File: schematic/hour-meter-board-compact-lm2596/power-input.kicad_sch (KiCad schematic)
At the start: 24 parts, among them J101 VIN 9-36V, U101 LM2596S-ADJ

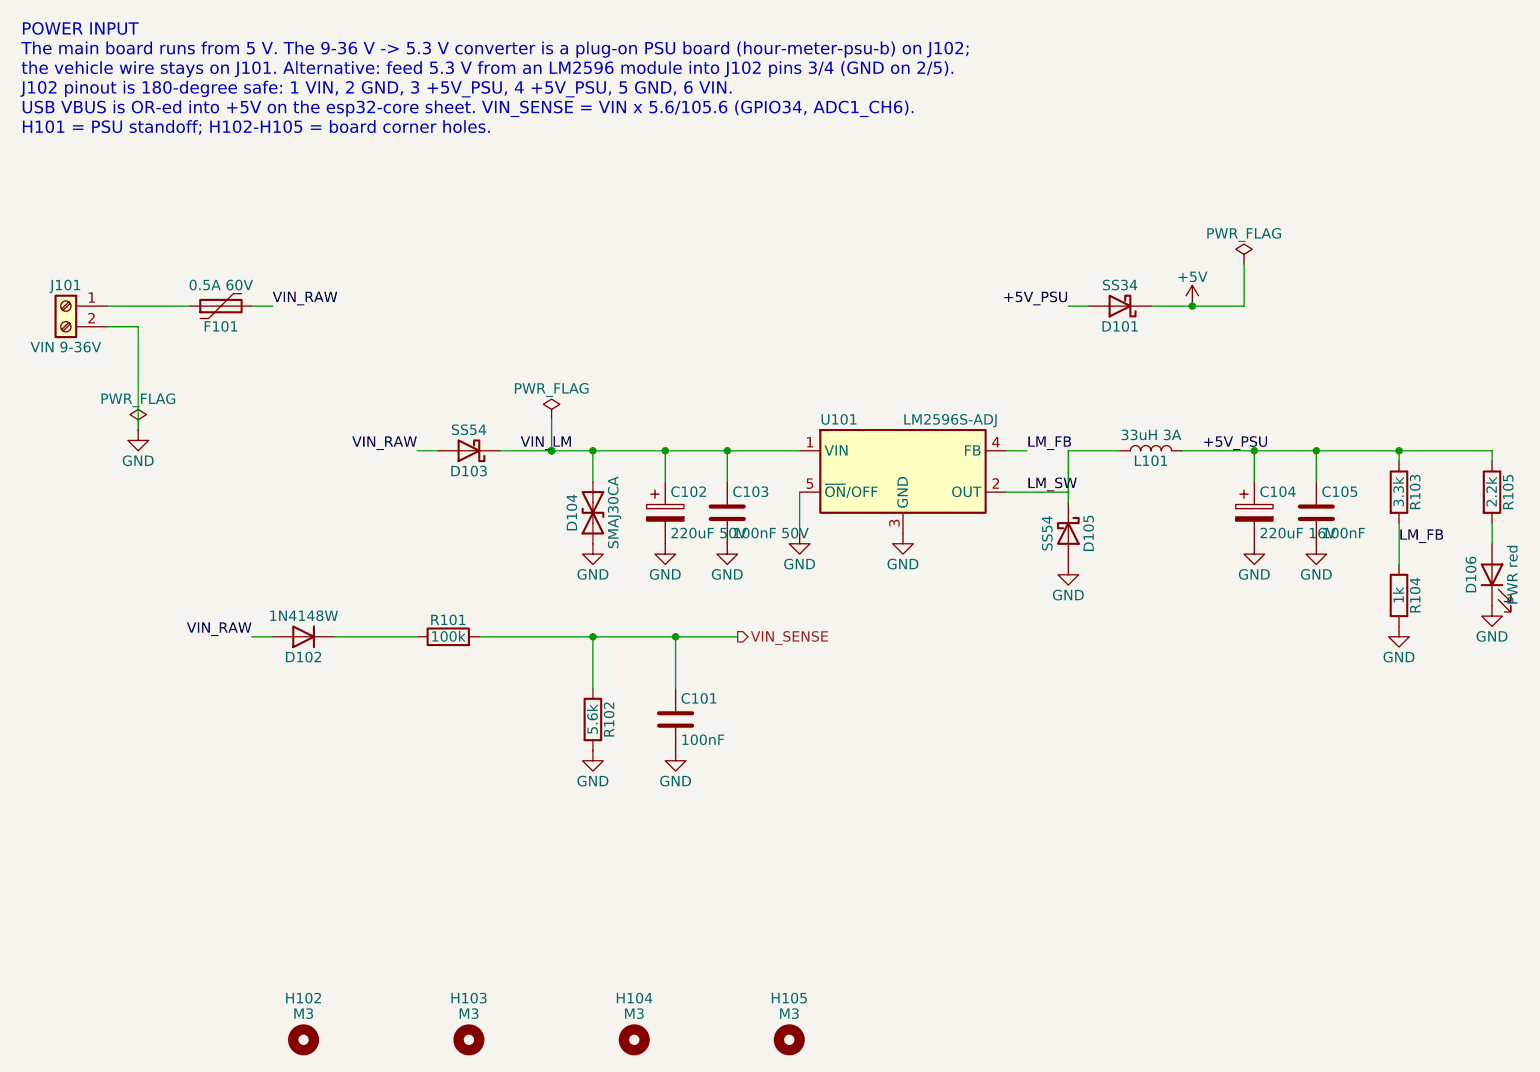
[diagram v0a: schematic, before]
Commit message: feat(pcb): use JST VH field connectors on the LM2596 compact board
- J101 (VIN 9-30V), J301 (vehicle IN), J701 (RS485) and J801 (UART) are
  latching JST VH headers instead of screw terminals and JST XH
- add TP101 VIN solder pads in parallel with J101
- GPS J802 becomes a 1x5 male pin header
- re-route the board (U203 VBUS escape fixed by re-routing the USB and
  ESP32 lines under it) and regenerate the JLCPCB order files
- tools-pcb.py: `models` command fetches the JLCPCB/EasyEDA STEP models;
  the downloaded 3d/ folders are git-ignored
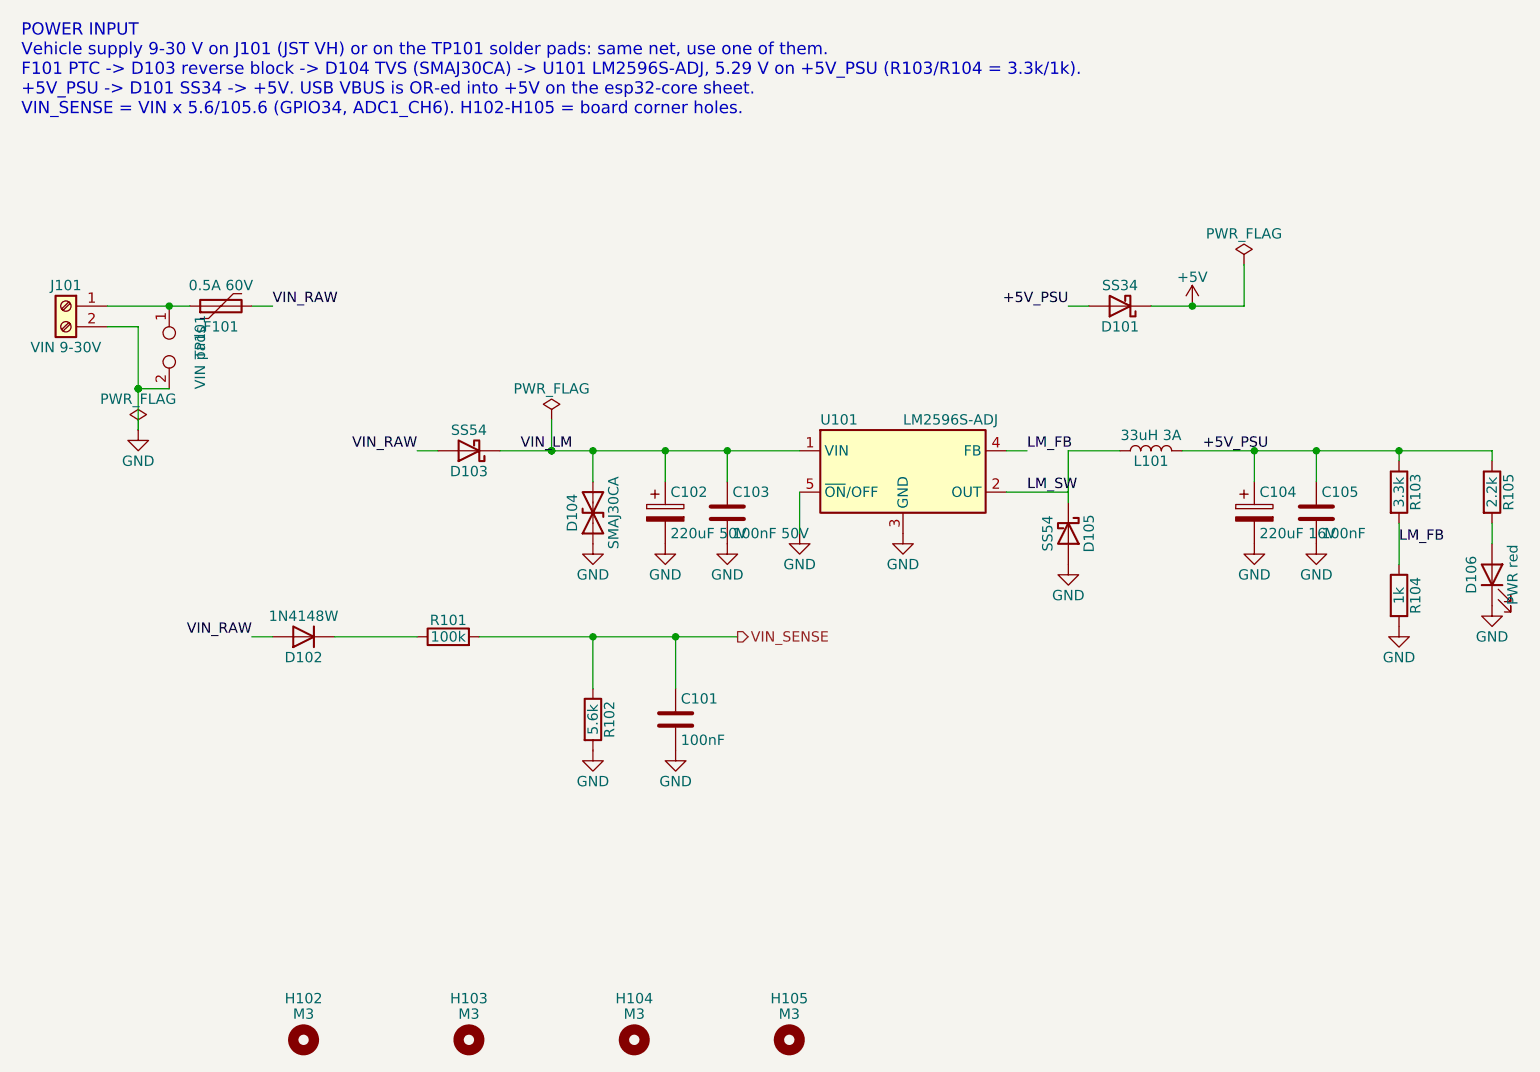
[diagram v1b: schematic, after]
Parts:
- added TP101: VIN pads, TestPoint:TestPoint_2Pads_Pitch5.08mm_Drill1.3mm, symbol Connector:TestPoint_2Pole
- J101: value VIN 9-36V -> VIN 9-30V; footprint TerminalBlock_Phoenix:TerminalBlock_Phoenix_MKDS-1,5-2-5.08_1x02_P5.08mm_Horizontal -> Connector_JST:JST_VH_B2P-VH_1x02_P3.96mm_Vertical; LCSC C474952 -> C160315; MPN KF128-5.08-2P-AA -> B2P-VH(LF)(SN)
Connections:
- net GND: now also TP101.2
- net at F101.1, J101.1 (Pin_1): now also TP101.1
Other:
- note added: "POWER INPUT Vehicle supply 9-30 V on J101 (JST VH) or on the TP101 solder pads: same net, use one of them. F101 PTC -> D103 reverse block -> D104 TVS (SMAJ30CA) -> U101 LM2596S-ADJ, 5.29 V on +5V_PSU (R103/R104 = 3.3k/1k). +5V_PSU -> D101 SS34 -> +5V. USB VBUS is OR-ed into +5V on the esp32-core sheet. VIN_SENSE = VIN x 5.6/105.6 (GPIO34, ADC1_CH6). H102-H105 = board corner holes."
- note removed: "POWER INPUT The main board runs from 5 V. The 9-36 V -> 5.3 V converter is a plug-on PSU board (hour-meter-psu-b) on J102; the vehicle wire stays on J101. Alternative: feed 5.3 V from an LM2596 module into J102 pins 3/4 (GND on 2/5). J102 pinout is 180-degree safe: 1 VIN, 2 GND, 3 +5V_PSU, 4 +5V_PSU, 5 GND, 6 VIN. USB VBUS is OR-ed into +5V on the esp32-core sheet. VIN_SENSE = VIN x 5.6/105.6 (GP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"
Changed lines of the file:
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@@
 		(diameter 0)
 	)
+	(junction
+		(at 43.18 59.69)
+		(diameter 0)
+	)
+	(junction
+		(at 39.37 69.85)
+		(diameter 0)
+	)
+	(junction
+		(at 39.37 69.85)
+		(diameter 0)
+	)
 	(wire
 		(pts
@@
 		)
 	)
-	(text "POWER INPUT\nThe main board runs from 5 V. The 9-36 V -> 5.3 V converter is a plug-on PSU board (hour-meter-psu-b) on J102;\nthe vehicle wire stays on J101. Alternative: feed 5.3 V from an LM2596 module into J102 pins 3/4 (GND on 2/5).\nJ102 pinout is 180-degree safe: 1 VIN, 2 GND, 3 +5V_PSU, 4 +5V_PSU, 5 GND, 6 VIN.\nUSB VBUS is OR-ed into +5V on the esp32-core sheet. VIN_SENSE = VIN x 5.6/105.6 (GPIO34, ADC1_CH6).\nH101 = PSU standoff; H102-H105 = board corner holes."
+	(wire
+		(pts
+			(xy 43.18 69.85)
+			(xy 39.37 69.85)
+		)
+	)
+	(text "POWER INPUT\nVehicle supply 9-30 V on J101 (JST VH) or on the TP101 solder pads: same net, use one of them.\nF101 PTC -> D103 reverse block -> D104 TVS (SMAJ30CA) -> U101 LM2596S-ADJ, 5.29 V on +5V_PSU (R103/R104 = 3.3k/1k).\n+5V_PSU -> D101 SS34 -> +5V. USB VBUS is OR-ed into +5V on the esp32-core sheet.\nVIN_SENSE = VIN x 5.6/105.6 (GPIO34, ADC1_CH6). H102-H105 = board corner holes."
 		(at 25 25 0)
 		(effects
@@
 			)
 		)
-		(property "Value" "VIN 9-36V"
+		(property "Value" "VIN 9-30V"
 			(at 30.48 64.77 0)
 			(effects
@@
 			)
 		)
-		(property "Footprint" "TerminalBlock_Phoenix:TerminalBlock_Phoenix_MKDS-1,5-2-5.08_1x02_P5.08mm_Horizontal"
+		(property "Footprint" "Connector_JST:JST_VH_B2P-VH_1x02_P3.96mm_Vertical"
 			(at 30.48 59.69 0)
 			(hide yes)
@@
 			)
 		)
-		(property "LCSC" "C474952"
+		(property "LCSC" "C160315"
 			(at 30.48 59.69 0)
 			(hide yes)
@@
 			)
 		)
-		(property "MPN" "KF128-5.08-2P-AA"
+		(property "MPN" "B2P-VH(LF)(SN)"
 			(at 30.48 59.69 0)
 			(hide yes)
@@
 					(unit 1)
 				)
+			)
+		)
+	)
+	(symbol
+		(lib_id "Connector:TestPoint_2Pole")
+		(at 43.18 64.77 270)
+		(unit 1)
+		(in_bom yes)
+		(on_board yes)
+		(dnp no)
+		(property "Reference" "TP101"
+			(at 46.99 63.5 0)
+			(effects
+				(font
+					(size 1.27 1.27)
+				)
+			)
+		)
+		(property "Value" "VIN pads"
+			(at 46.99 66.04 0)
+			(effects
+				(font
+					(size 1.27 1.27)
+				)
+			)
+		)
+		(property "Footprint" "TestPoint:TestPoint_2Pads_Pitch5.08mm_Drill1.3mm"
+			(at 43.18 64.77 0)
+			(hide yes)
+			(effects
+				(font
+					(size 1.27 1.27)
+				)
+			)
+		)
+		(property "Datasheet" ""
+			(at 43.18 64.77 0)
+			(hide yes)
+			(effects
+				(font
+					(size 1.27 1.27)
+				)
+			)
+		)
+		(property "Description" "2-polar test point"
+			(at 43.18 64.77 0)
+			(hide yes)
+			(effects
+				(font
+					(size 1.27 1.27)
+				)
+			)
+		)
+		(instances
+			(project "hour-meter-board-compact-lm2596"
+				(path "/59d580f2-180f-4c52-8215-2508c8a389e3/7d36e08f-90ac-4d15-b354-173e665395cb"
+					(reference "TP101")
+					(unit 1)
+				)
